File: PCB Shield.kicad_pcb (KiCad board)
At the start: 2 copper layers, 92 x 99 mm, 53 parts, among them J1 Conn_1to20, J10 TB002-500-02BE, J11 TB002-500-02BE, J12 TB002-500-02BE, J13 TB002-500-02BE, J14 TB002-500-02BE, J15 TB002-500-02BE, J16 TB002-500-02BE, J2 Conn_01x08_Socket, J3 Conn_1to20, J4 Conn_20to49, J5 Conn_20to49, J6 Conn_01x04_Socket, J7 Conn_01x04_Socket, J8 OSTT7020150, J9 TB002-500-02BE, Q1 IRLML2502TRPBF, SW1 C1353VQNAA, U1 ESDA6V1L, U2 SO14_DIO

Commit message: FINISHED
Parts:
- J2: footprint Connector_PinSocket_2.54mm:PinSocket_1x08_P2.54mm_Vertical -> 196_Project_Footprints:PinSocket_1x08_P2.54mm_Vertical
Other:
- outline, holes or cut-outs redrawn
- board text added: "+ -"
- board text added: "+3v3"
- board text added: "1"
- board text added: "10"
- board text added: "11"
- board text added: "12"
- board text added: "13"
- board text added: "14"
- board text added: "15"
- board text added: "16"
- board text added: "17"
- board text added: "18"
- board text added: "1Y"
- board text added: "2"
- board text added: "21"
- board text added: "26"
- board text added: "2Y"
- board text added: "3"
- board text added: "33"
- board text added: "34"
- board text added: "35"
- board text added: "36"
- board text added: "37"
- board text added: "38"
- board text added: "39"
- board text added: "3V3"
- board text added: "3Y"
- board text added: "4"
- board text added: "40"
- board text added: "41"
- board text added: "42"
- board text added: "43"
- board text added: "44"
- board text added: "45"
- board text added: "46"
- board text added: "47"
- board text added: "48"
- board text added: "4Y"
- board text added: "5"
- board text added: "5V"
- board text added: "6"
- board text added: "7"
- board text added: "8"
- board text added: "9"
- board text added: "CS"
- board text added: "GND"
- board text added: "IRQ"
- board text added: "MISO"
- board text added: "MOSI"
- board text added: "RST"
- board text added: "SCL"
- board text added: "SCLK"
- board text added: "SDA"
- board text added: "brightness"
- board text added: "switch"
- board text added: "volume"

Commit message: finished finally finally
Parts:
- added ?: LOGO, LOGO, B.Cu at (186.1, 87.7)
- added ?: LOGO, LOGO, B.Cu at (236.6, 145.9)
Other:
- board text added: "GHaresco"

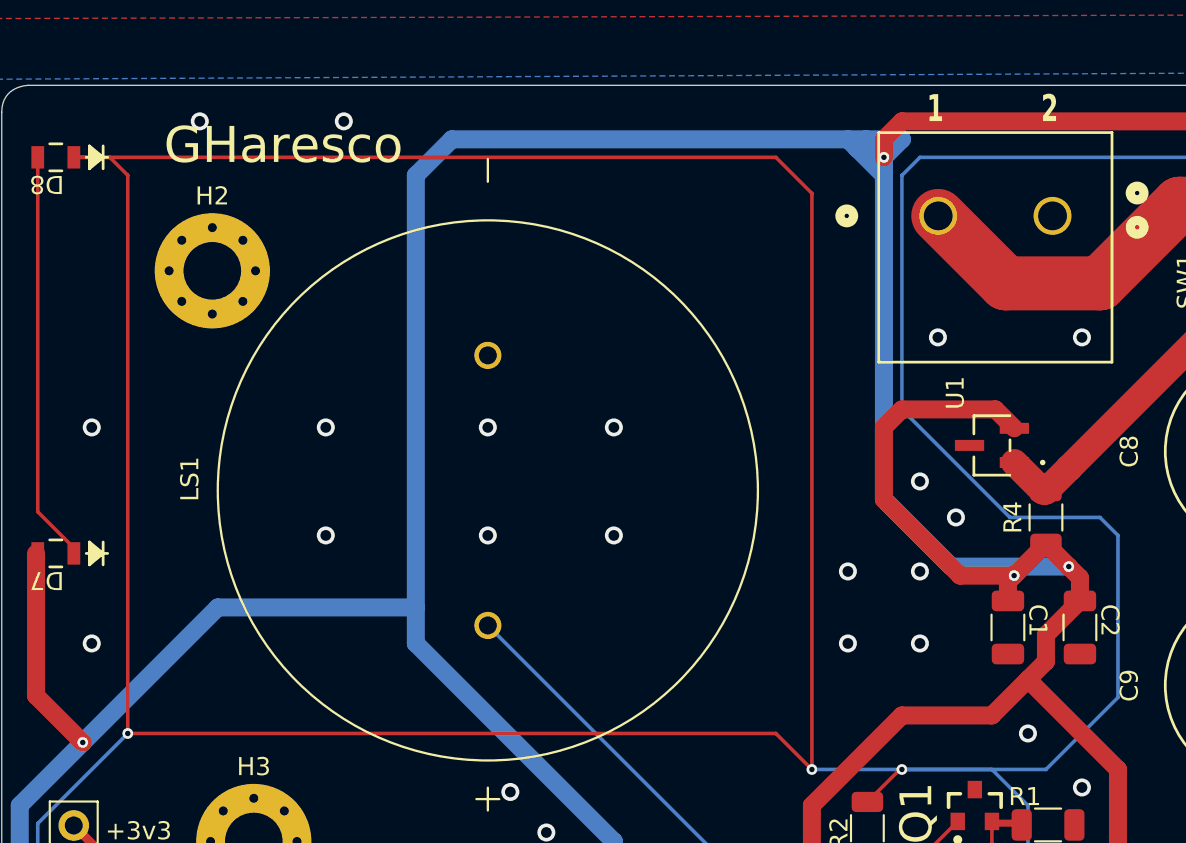
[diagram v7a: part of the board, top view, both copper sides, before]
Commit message: swapped out out of stock / weird order components
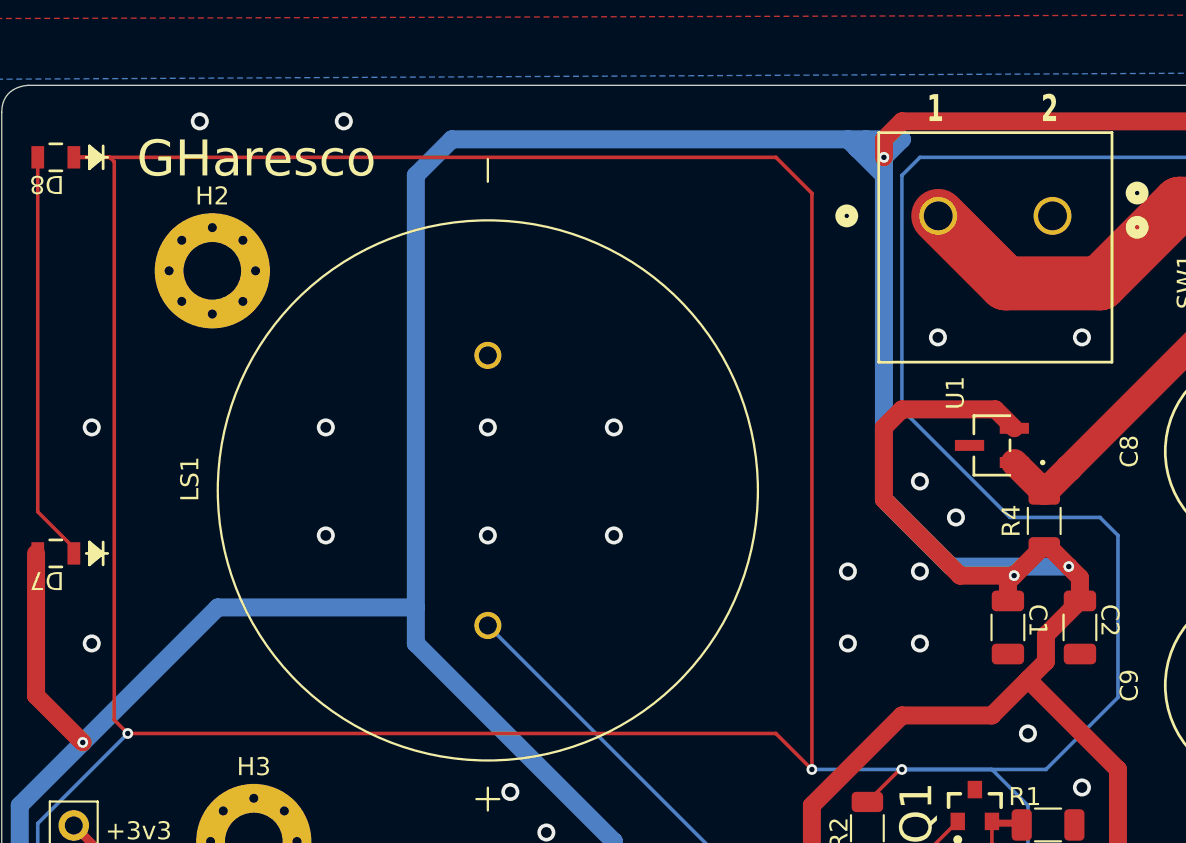
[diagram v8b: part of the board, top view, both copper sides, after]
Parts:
- Q1: value IRLML2502TRPBF -> DMN2075U-7
- R4: value R_Small_US -> 0
- U2: value SO14_DIO -> 74AHCT125S14-13
- moved ? 1.87 mm to (238.5, 146.0)
- moved R4 0.22 mm to (216.9, 90.2)
